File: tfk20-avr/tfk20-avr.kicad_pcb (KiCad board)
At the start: 2 copper layers, 76.2 x 114.3 mm, 122 parts, among them J1 USB_C_Receptacle_USB2.0, J2 AVR-ISP-6, SW1 Reset, U1 ATmega32U4-AU, U2 IS31FL3733-TQ, Y1 16MHz

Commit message: Place all footprints on PCB
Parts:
- C1, C11, C12, C13, C14, C15, C16, C17, C18, C19, C2, C20, C21, C22, C23, C3, C4, C5, C7, D1, D10, D11, D12, D13, D14, D15, D16, D17, D18, D19, D2, D20, D21, D22, D23, D24, D5, D6, D7, D8, D9, F1, R10, R11, R12, R13, R5, R6, R7, R9: moved to B.Cu
- moved J2 161.6 mm to (102.6, 162.3)
- moved C11 154.3 mm to (84.1, 96.0), turned to 90 degrees
- moved C13 143.1 mm to (84.1, 115.1), turned to 90 degrees
- moved D8 141.0 mm to (84.9, 90.5), turned to 90 degrees
- moved D2 138.6 mm to (88.9, 69.8)
- moved C15 138.5 mm to (84.1, 153.2), turned to 90 degrees
- moved D12 138.3 mm to (84.9, 109.5), turned to 90 degrees
- moved D3 134.6 mm to (88.9, 71.4), turned to 270 degrees
- moved D19 131.4 mm to (84.9, 147.6), turned to 90 degrees
- moved R3 131.0 mm to (90.2, 62.1), turned to 270 degrees
- moved R6 130.6 mm to (108.0, 97.0)
- moved D1 129.3 mm to (81.2, 59.2), turned to 180 degrees
- moved R7 128.4 mm to (135.5, 144.7), turned to 180 degrees
- moved D15 127.7 mm to (84.9, 128.6), turned to 90 degrees
- moved R2 127.0 mm to (87.6, 62.1), turned to 90 degrees
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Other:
- board size 76.2 x 114.3 mm -> 76.2 x 120.7 mm

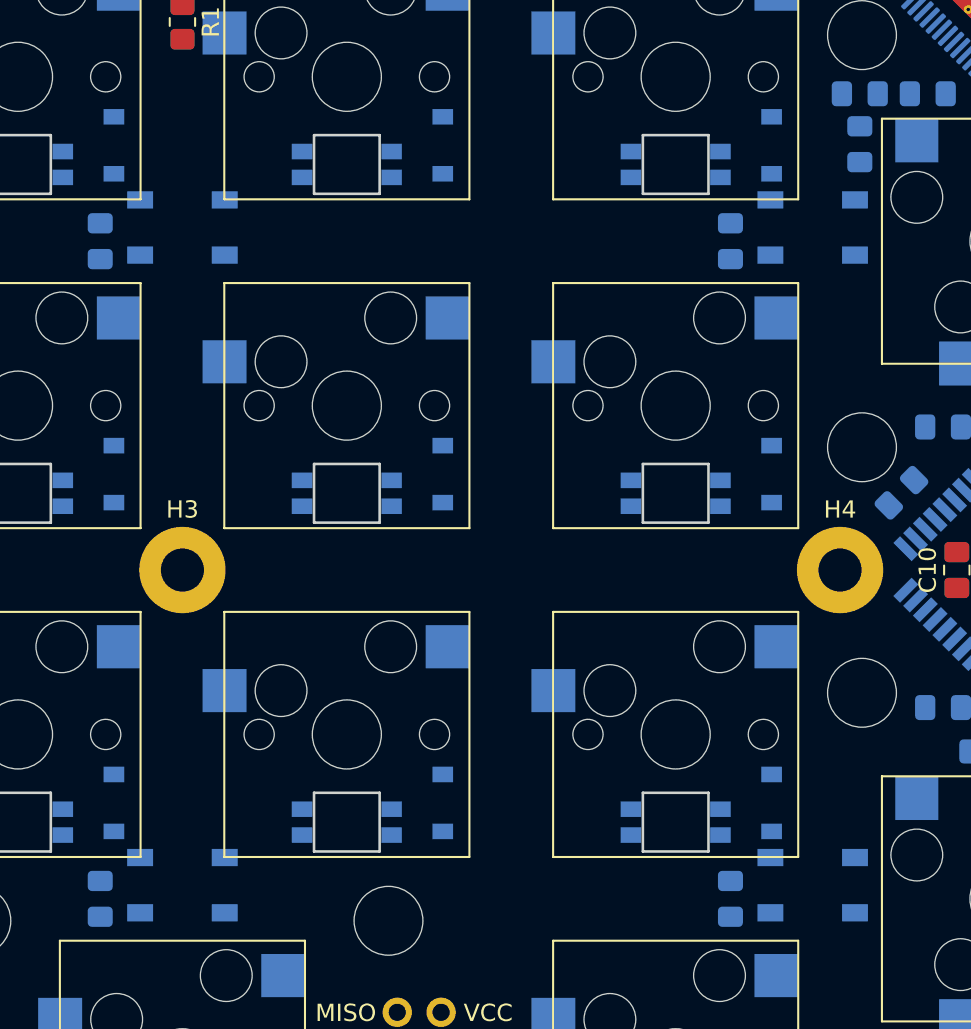
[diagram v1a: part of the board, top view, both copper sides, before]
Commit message: Fix clearance and courtyard issues
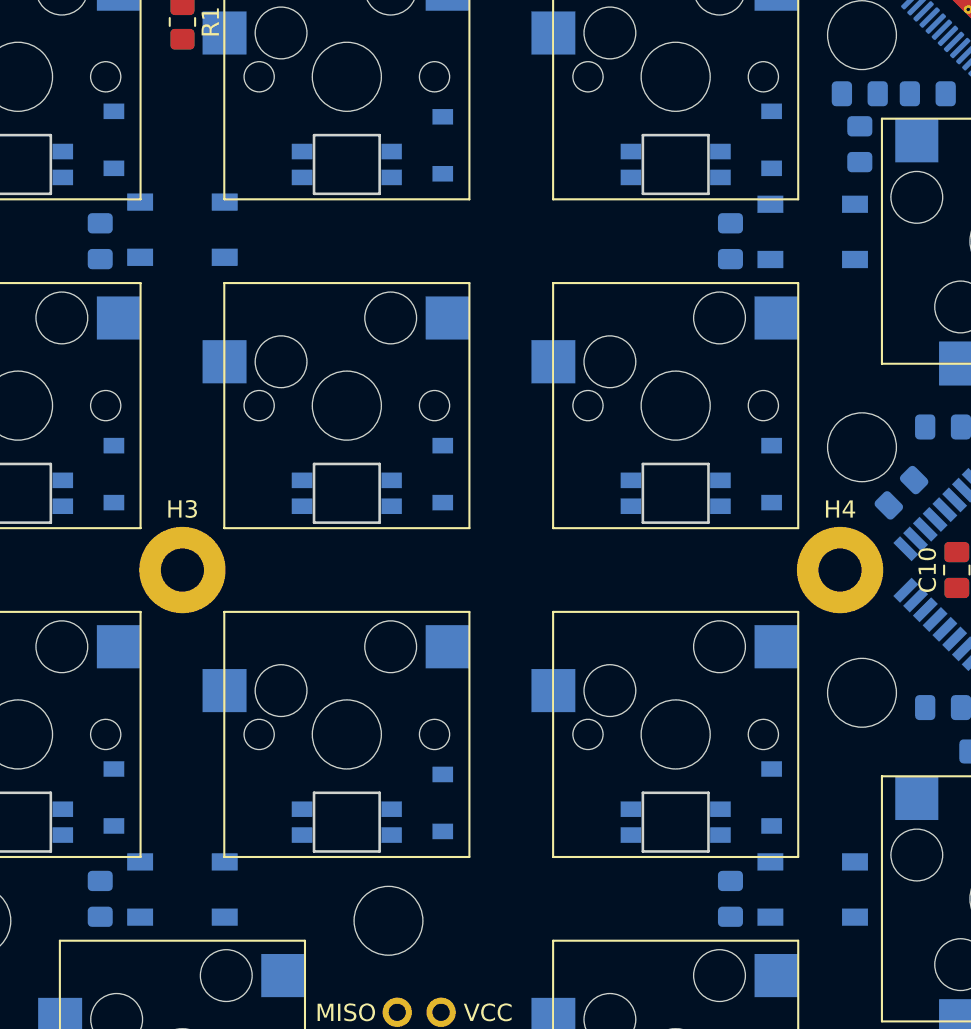
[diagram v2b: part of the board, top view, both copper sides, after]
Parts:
- moved D12 0.32 mm to (84.9, 109.2)
- moved D14 0.32 mm to (123.0, 109.2)
- moved D19 0.32 mm to (84.9, 147.3)
- moved D21 0.32 mm to (123.0, 147.3)
- moved D28 0.25 mm to (125.4, 114.6)
- moved D29 0.25 mm to (88.9, 152.7)
- moved D30 0.25 mm to (125.4, 152.7)
- moved D27 0.13 mm to (88.9, 114.4)
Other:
- net class Default: clearance 0.2 -> 0.15
- net class Power: clearance 0.2 -> 0.14
- rule trace_clearance: 0.2 -> 0.15
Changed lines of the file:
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@@
   (setup
     (last_trace_width 0.25)
-    (trace_clearance 0.2)
+    (trace_clearance 0.15)
     (zone_clearance 0.508)
     (zone_45_only no)
@@
   (net 108 "Net-(U2-Pad1)")
   (net_class Default "This is the default net class."
-    (clearance 0.2)
+    (clearance 0.15)
     (trace_width 0.25)
     (via_dia 0.8)
@@
   )
   (net_class Power ""
-    (clearance 0.2)
+    (clearance 0.14)
     (trace_width 0.381)
     (via_dia 0.8)
@@
   )
   (module LED_SMD:LED_WS2812B_PLCC4_5.0x5.0mm_P3.2mm (layer B.Cu)
-    (at 125.4125 152.4)
+    (at 125.4125 152.654)
     (descr https://cdn-shop.adafruit.com/datasheets/WS2812B.pdf)
     (tags "LED RGB NeoPixel")
@@
   )
   (module LED_SMD:LED_WS2812B_PLCC4_5.0x5.0mm_P3.2mm (layer B.Cu)
-    (at 88.9 152.4)
+    (at 88.9 152.654)
     (descr https://cdn-shop.adafruit.com/datasheets/WS2812B.pdf)
     (tags "LED RGB NeoPixel")
@@
   )
   (module LED_SMD:LED_WS2812B_PLCC4_5.0x5.0mm_P3.2mm (layer B.Cu)
-    (at 125.4125 114.3)
+    (at 125.4125 114.554)
     (descr https://cdn-shop.adafruit.com/datasheets/WS2812B.pdf)
     (tags "LED RGB NeoPixel")
@@
   )
   (module LED_SMD:LED_WS2812B_PLCC4_5.0x5.0mm_P3.2mm (layer B.Cu)
-    (at 88.9 114.3)
+    (at 88.9 114.427)
     (descr https://cdn-shop.adafruit.com/datasheets/WS2812B.pdf)
     (tags "LED RGB NeoPixel")
@@
   )
   (module Diode_SMD:D_SOD-123 (layer B.Cu)
-    (at 123.03125 147.6375 90)
+    (at 123.03125 147.32 90)
     (descr SOD-123)
     (tags SOD-123)
@@
   )
   (module Diode_SMD:D_SOD-123 (layer B.Cu)
-    (at 84.93125 147.6375 90)
+    (at 84.93125 147.32 90)
     (descr SOD-123)
     (tags SOD-123)
@@
   )
   (module Diode_SMD:D_SOD-123 (layer B.Cu)
-    (at 123.03125 109.5375 90)
+    (at 123.03125 109.22 90)
     (descr SOD-123)
     (tags SOD-123)
@@
   )
   (module Diode_SMD:D_SOD-123 (layer B.Cu)
-    (at 84.93125 109.5375 90)
+    (at 84.93125 109.22 90)
     (descr SOD-123)
     (tags SOD-123)

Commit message: Begin north-facing LED layout
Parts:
- removed H3: MountingHole, MountingHole:MountingHole_2.5mm_Pad
- added He: MountingHole, MountingHole:MountingHole_2.5mm_Pad, F.Cu at (-104.0, 116.7)
- C1, C11, C12, C13, C14, C15, C16, C17, C18, C19, C2, C20, C21, C22, C23, C3, C4, C5, C7, D1, D10, D11, D12, D13, D14, D15, D16, D17, D18, D19, D2, D20, D21, D22, D23, D24, D4, D5, D6, D7, D8, D9, F1, R10, R11, R12, R13, R5, R6, R7, R9: moved to F.Cu
- C10, C9, H5, H6, H7, Y1: moved to B.Cu
- moved C9 210.5 mm to (-66.7, 104.0)
- moved Y1 202.7 mm to (-62.7, 104.0), turned to 0 degrees
- moved D26 197.0 mm to (-68.3, 79.4)
- moved D29 195.1 mm to (-104.0, 123.0)
- moved C10 194.8 mm to (-58.7, 104.0), turned to 270 degrees
- moved D28 194.3 mm to (-68.3, 98.4)
- moved U1 194.0 mm to (-55.6, 116.7), turned to 45 degrees
- moved D34 193.7 mm to (-56.4, 50.0), turned to 0 degrees
- moved D38 193.7 mm to (-56.4, 69.1), turned to 0 degrees
- moved D45 193.7 mm to (-56.4, 97.6), turned to 90 degrees
- moved D49 193.7 mm to (-104.0, 145.3), turned to 0 degrees
- moved D51 193.7 mm to (-56.4, 135.7), turned to 90 degrees
- moved H1 193.7 mm to (-104.0, 59.5)
- moved H5 193.7 mm to (-56.4, 97.6), turned to 90 degrees
- moved H6 193.7 mm to (-56.4, 135.7), turned to 90 degrees
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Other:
- board size 76.2 x 120.7 mm -> 76.2 x 115.9 mm
- net class Default: via_dia 0.8 -> 0.6; via_drill 0.4 -> 0.3
- net class Power: clearance 0.14 -> 0.15

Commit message: Finish north-facing LED footprint layout
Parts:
- removed He: MountingHole, MountingHole:MountingHole_2.5mm_Pad
- added H3: MountingHole, MountingHole:MountingHole_2.5mm_Pad, F.Cu at (126.2, 115.1)
- C1, C11, C12, C13, C14, C15, C16, C17, C18, C19, C2, C20, C21, C22, C23, C3, C4, C5, C6, C7, C8, D1, D10, D11, D12, D13, D14, D15, D16, D17, D18, D19, D2, D20, D21, D22, D23, D24, D3, D4, D5, D6, D7, D8, D9, F1, J2, R1, R10, R11, R12, R13, R2, R3, R4, R5, R6, R7, R8, R9: moved to B.Cu
- H1: value Case -> MountingHole
- H2: value MountingHole -> Case
- moved C10 230.2 mm to (171.4, 102.4)
- moved C9 230.2 mm to (163.5, 102.4)
- moved D25 230.2 mm to (127.8, 77.8)
- moved D26 230.2 mm to (161.9, 77.8)
- moved D27 230.2 mm to (127.8, 96.8)
- moved D28 230.2 mm to (161.9, 96.8)
- moved D29 230.2 mm to (126.2, 121.4)
- moved D30 230.2 mm to (168.3, 127.8)
- moved D31 230.2 mm to (116.7, 48.4)
- moved D32 230.2 mm to (135.7, 48.4)
- moved D33 230.2 mm to (154.8, 48.4)
- moved D34 230.2 mm to (173.8, 48.4)
- moved D35 230.2 mm to (116.7, 67.5)
- moved D36 230.2 mm to (135.7, 67.5)
- moved D37 230.2 mm to (154.8, 67.5)
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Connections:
- H1 pad 1: Net-(D3-Pad2) -> (no net)
- H2 pad 1: (no net) -> Net-(D3-Pad2)

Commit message: Continue routing
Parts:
- C15, C16, D29, D30: moved to F.Cu
- moved D29 101.9 mm to (223.4, 91.0)
- moved C15 98.4 mm to (219.2, 102.4)
- moved C16 78.7 mm to (230.0, 92.2), turned to 0 degrees
- moved C11 64.8 mm to (163.4, 134.1)
- moved D25 64.4 mm to (168.3, 127.9)
- moved D30 62.9 mm to (223.4, 97.6)
- moved D26 56.3 mm to (126.2, 121.3)
- moved C12 51.7 mm to (119.9, 115.1), turned to 180 degrees
- moved D28 39.1 mm to (127.8, 77.8)
- moved C14 38.0 mm to (127.4, 82.9)
- moved C18 18.0 mm to (167.3, 89.4), turned to 270 degrees
- moved D1 16.7 mm to (124.6, 64.3), turned to 270 degrees
- moved F1 12.7 mm to (127.8, 64.3)
- moved C21 10.3 mm to (180.7, 79.1), turned to 0 degrees
- moved C10 7.87 mm to (163.6, 102.4)
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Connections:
- net Net-(D1-Pad1) renamed VBUS
- net Net-(R5-Pad2) renamed /MCU_USB_D+
- net Net-(R6-Pad2) renamed /MCU_USB_D-
- C10 pad 2: Net-(C10-Pad2) -> GND
- C9 pad 1: Net-(C10-Pad2) -> GND
- Y1 pad 4: Net-(C10-Pad2) -> GND
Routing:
- net +5V: track 0.00 -> 333.0 mm, vias 0 -> 2
- net /MCU_USB_D-: track 0.00 -> 81.7 mm, vias 0 -> 2
- net /MCU_USB_D+: track 0.00 -> 80.4 mm, vias 0 -> 2
- net Net-(D25-Pad2): track 0.00 -> 39.2 mm, vias 0 -> 2
- net /IN_USB_D+: track 0.00 -> 38.6 mm, vias 0 -> 3
- net /IN_USB_D-: track 0.00 -> 38.6 mm, vias 0 -> 3
- net /SHIELD: track 0.00 -> 36.5 mm
- net VBUS: track 0.00 -> 32.4 mm
- net /RGB_MATRIX_SCL: track 0.00 -> 28.1 mm, vias 0 -> 2
- net /RGB_MATRIX_SDA: track 0.00 -> 27.2 mm, vias 0 -> 2
- net Net-(D26-Pad2): track 0.00 -> 25.2 mm
- net /RGB_LIGHT: track 0.00 -> 20.7 mm, vias 0 -> 2
- net Net-(D27-Pad2): track 0.00 -> 17.9 mm, vias 0 -> 2
- net /XTAL2: track 0.00 -> 15.5 mm
- net Net-(C7-Pad1): track 0.00 -> 10.6 mm
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- added copper zone on B.Cu, net GND
- added copper zone on F.Cu, net GND

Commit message: Continue routing
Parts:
- C15, C16, D29, D30: moved to B.Cu
- moved C16 70.2 mm to (160.5, 102.0)
- moved D29 62.9 mm to (161.9, 77.8)
- moved C15 62.0 mm to (160.4, 82.9)
- moved D30 61.5 mm to (161.9, 96.8)
- moved C11 3.06 mm to (163.7, 137.2), turned to 270 degrees
- moved D22 2.25 mm to (117.5, 146.8), turned to 270 degrees
- moved D15 0.79 mm to (112.7, 115.1)
- moved D14 0.79 mm to (150.8, 96.0)
- moved C6 0.25 mm to (141.4, 42.2)
- moved C8 0.25 mm to (166.1, 42.2)
- moved D3 0.25 mm to (165.0, 46.6)
- moved R4 0.25 mm to (143.6, 42.2)
- moved R8 0.25 mm to (163.8, 42.2)
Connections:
- U1 pad 27: /COL_3 -> /COL_2
- U1 pad 28: /COL_0 -> /COL_1
- U1 pad 29: /COL_1 -> /COL_0
- U1 pad 30: /COL_2 -> /COL_3
- U1 pad 36: /ROW_5 -> /ROW_0
- U1 pad 37: /ROW_4 -> /ROW_1
- U1 pad 38: /ROW_3 -> /ROW_2
- U1 pad 39: /ROW_2 -> /ROW_3
- U1 pad 40: /ROW_1 -> /ROW_4
- U1 pad 41: /ROW_0 -> /ROW_5
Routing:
- net /COL_0: track 0.00 -> 165.4 mm, vias 0 -> 4
- net /tfk20 RGB Matrix/SW1: track 0.00 -> 148.4 mm, vias 0 -> 4
- net /COL_2: track 0.00 -> 137.7 mm, vias 0 -> 11
- net /RESET: track 5.30 -> 142.1 mm, vias 1 -> 3
- net /COL_1: track 0.00 -> 136.6 mm, vias 0 -> 8
- net /ROW_0: track 0.00 -> 127.1 mm, vias 0 -> 6
- net /ROW_5: track 0.00 -> 91.2 mm, vias 0 -> 2
- net /COL_3: track 0.00 -> 86.1 mm, vias 0 -> 6
- net GND: track 7.80 -> 90.2 mm, vias 2 -> 15
- net /ROW_2: track 0.00 -> 80.5 mm, vias 0 -> 4
- net /ROW_1: track 0.00 -> 71.4 mm, vias 0 -> 4
- net /MISO: track 0.00 -> 54.0 mm, vias 0 -> 1
- net /ROW_4: track 0.00 -> 52.6 mm, vias 0 -> 4
- net /SCK: track 0.00 -> 51.1 mm, vias 0 -> 1
- net /MOSI: track 0.00 -> 49.5 mm, vias 0 -> 1
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
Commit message: Continue routing
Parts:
- moved R11 41.5 mm to (172.5, 87.6), turned to 180 degrees
- moved R10 39.8 mm to (167.4, 87.6), turned to 0 degrees
- moved C17 1.27 mm to (165.1, 90.7)
- moved C18 1.27 mm to (167.3, 90.7)
- moved C22 1.27 mm to (171.6, 90.7)
- moved C23 1.27 mm to (169.4, 90.7)
- moved C12 0.46 mm to (119.5, 115.3)
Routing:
- net /tfk20 RGB Matrix/SW9: track 0.00 -> 141.4 mm, vias 0 -> 6
- net /tfk20 RGB Matrix/SW7: track 0.00 -> 139.8 mm, vias 0 -> 9
- net /tfk20 RGB Matrix/SW3: track 20.5 -> 151.3 mm, vias 2 -> 9
- net /tfk20 RGB Matrix/SW8: track 0.00 -> 121.7 mm, vias 0 -> 14
- net /tfk20 RGB Matrix/CS1: track 1.46 -> 92.6 mm, vias 1 -> 3
- net /tfk20 RGB Matrix/SW2: track 0.00 -> 71.6 mm, vias 0 -> 4
- net /tfk20 RGB Matrix/CS7: track 1.39 -> 49.3 mm, vias 1 -> 6
- net /tfk20 RGB Matrix/CS5: track 1.20 -> 47.1 mm, vias 1 -> 2
- net /ROW_3: track 31.3 -> 74.4 mm, vias 2 -> 4
- net /tfk20 RGB Matrix/SW4: track 0.00 -> 23.9 mm, vias 0 -> 2
- net /ROW_4: track 52.6 -> 75.7 mm, vias 4 -> 5
- net /tfk20 RGB Matrix/SW5: track 0.00 -> 21.2 mm, vias 0 -> 2
- net +5V: track 335.0 -> 319.4 mm
- net /tfk20 RGB Matrix/SW6: track 0.00 -> 14.0 mm, vias 0 -> 2
- net GND: track 90.2 -> 102.5 mm, vias 15 -> 17
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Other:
- copper layers 2 -> 4

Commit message: Continue routing
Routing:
- net /tfk20 RGB Matrix/CS5: track 47.1 -> 192.1 mm, vias 2 -> 11
- net /tfk20 RGB Matrix/CS2: track 1.69 -> 142.7 mm, vias 1 -> 19
- net /tfk20 RGB Matrix/SW5: track 21.2 -> 149.8 mm, vias 2 -> 18
- net /tfk20 RGB Matrix/SW6: track 14.0 -> 140.8 mm, vias 2 -> 15
- net /tfk20 RGB Matrix/CS3: track 1.68 -> 126.9 mm, vias 1 -> 9
- net /tfk20 RGB Matrix/CS6: track 0.00 -> 113.0 mm, vias 0 -> 14
- net /tfk20 RGB Matrix/SW4: track 23.9 -> 135.7 mm, vias 2 -> 16
- net /tfk20 RGB Matrix/CS8: track 0.00 -> 111.4 mm, vias 0 -> 10
- net /tfk20 RGB Matrix/SW2: track 71.6 -> 181.1 mm, vias 4 -> 12
- net /tfk20 RGB Matrix/SW9: track 141.4 -> 246.7 mm, vias 6 -> 8
- net /tfk20 RGB Matrix/CS7: track 49.3 -> 136.4 mm, vias 6 -> 16
- net /tfk20 RGB Matrix/SW7: track 139.8 -> 225.2 mm, vias 9 -> 12
- net /tfk20 RGB Matrix/SW8: track 121.7 -> 204.4 mm, vias 14 -> 20
- net /tfk20 RGB Matrix/CS1: track 92.6 -> 156.3 mm, vias 3 -> 9
- net /tfk20 RGB Matrix/CS4: track 0.00 -> 41.8 mm, vias 0 -> 2
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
